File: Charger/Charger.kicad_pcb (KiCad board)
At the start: 2 copper layers, 100 x 100 mm, 189 parts, among them J1 Bat_ballanser_conn, J2 Battery_conn, J3 Power_conn, J4 Screen_SPInCtrlnPwr_Conn, J5 User_Interface_Conn, J8 Temp_Sens_Conn, Q1 BC846BW, Q10 MJD45H11T4, Q11 MJD45H11T4, Q12 MJD45H11T4, Q13 BC846BW, Q14 MJD31CT4, Q15 BUJ302AD, Q16 BUJ302AD, Q17 IRF7404, Q18 IRF7404, Q19 BC846BW, Q2 BC846BW, Q3 BC846BW, Q4 MJD45H11T4, Q5 MJD45H11T4, Q6 MJD45H11T4, Q7 BC846BW, Q8 BC846BW, Q9 BC846BW, U1 LM2904, U10 MCP6001-OT, U12 ACS712xLCTR-20A, U13 MCP6004, U17 XL4015, U18 XL4015, U19 MCP6001-OT, U2 LM2904, U20 LM2575-12BU, U21 L7805, U22 LDI1117-3.3, U23 RaspberryPi_Pico, U24 CD4051B, U25 MCP6004, U3 LM2904, U4 LM2904, U5 LM2904, U6 LM2904

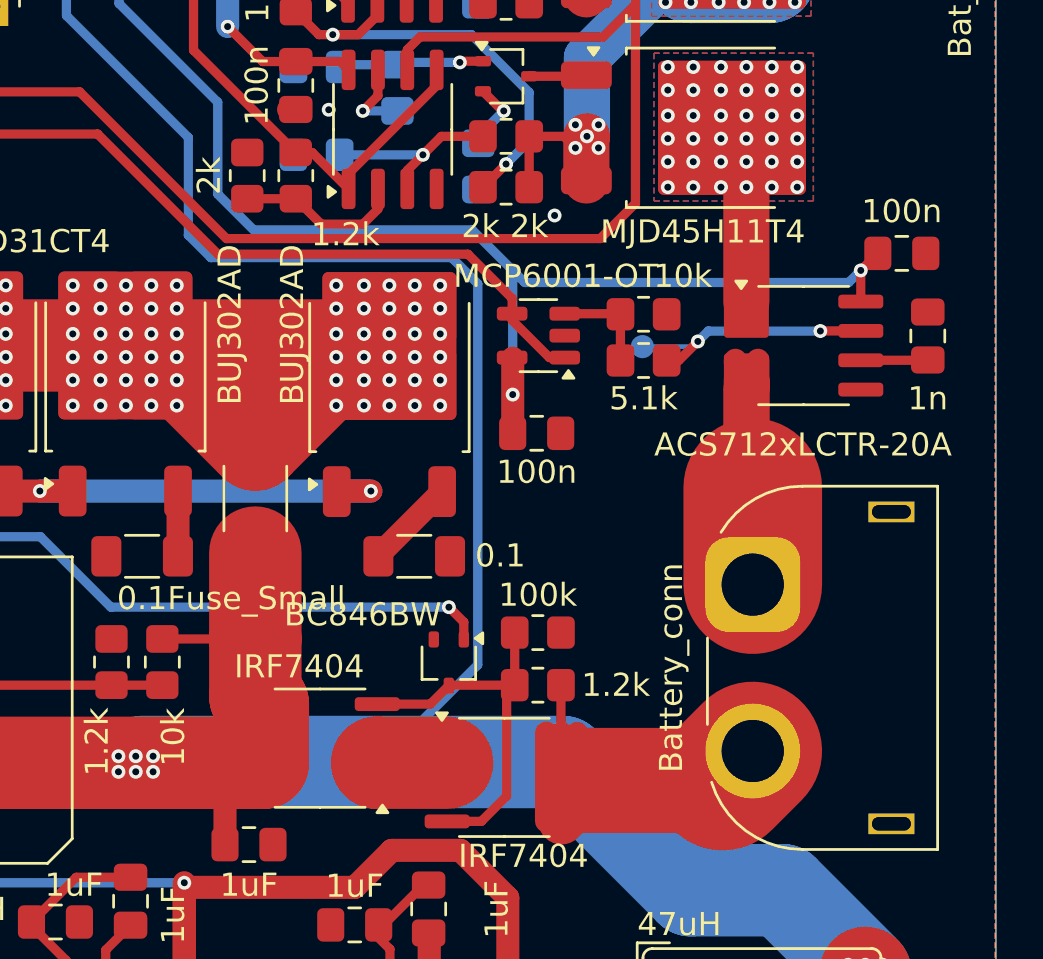
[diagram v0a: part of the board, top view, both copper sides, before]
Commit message: dodany hall od tylu i opisy
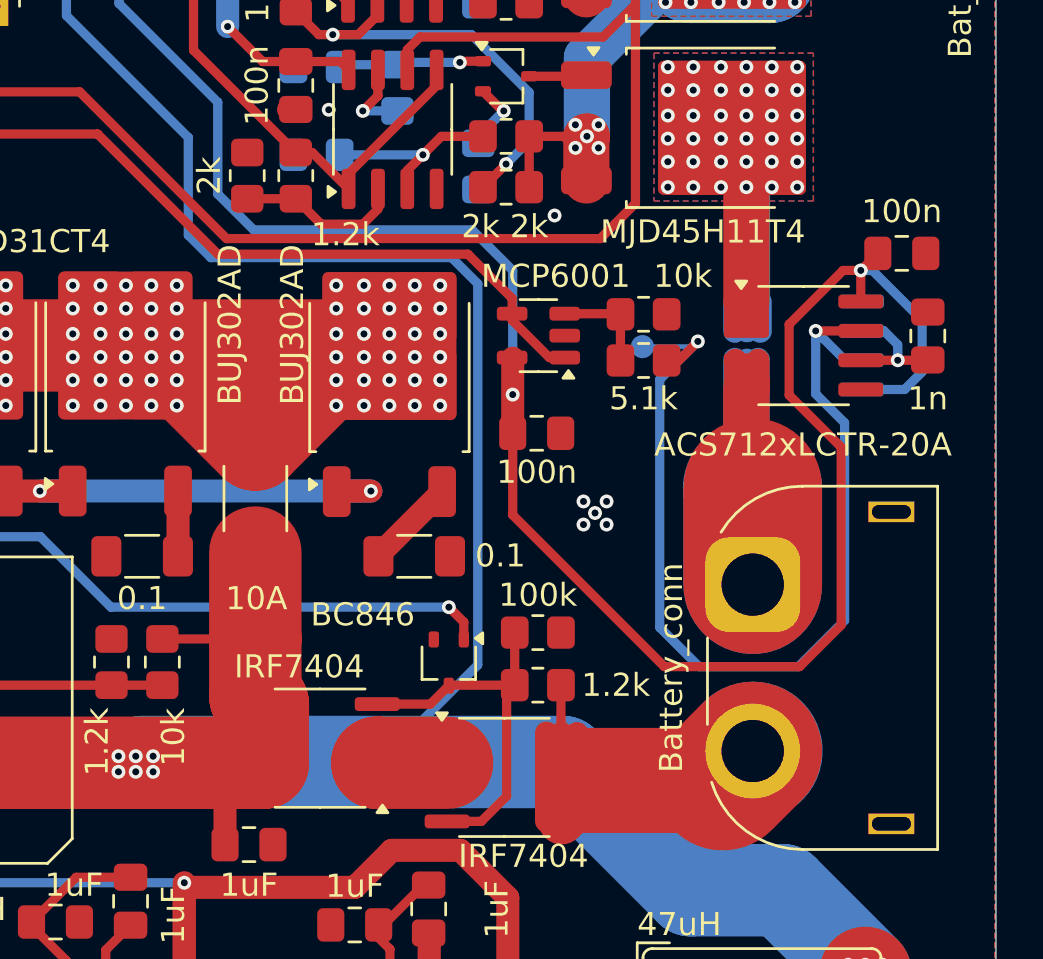
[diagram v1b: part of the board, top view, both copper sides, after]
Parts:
- added U7: ACS712xLCTR-20A, Package_SO:SOIC-8_3.9x4.9mm_P1.27mm, B.Cu at (184.7, 100.2)
- F2: value Fuse_Small -> 10A
- Q19: value BC846BW -> BC846
- U10: value MCP6001-OT -> MCP6001
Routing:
- net Net-(U12-VIOUT): track 11.4 -> 44.3 mm
- net +5V: track 282.8 -> 315.2 mm
- net /Pomiar pradu/BAT-: track 19.0 -> 31.4 mm
- net GND: track 48.0 -> 57.9 mm, vias 199 -> 204
- net Net-(U12-FILTER): track 2.91 -> 5.40 mm, vias 0 -> 1
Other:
- board text added: "+3.3V"
- board text added: "BL"
- board text added: "BTN_1"
- board text added: "BTN_2"
- board text added: "CS"
- board text added: "D/C"
- board text added: "ENC_CLK"
- board text added: "ENC_DT"
- board text added: "ENC_SW"
- board text added: "FMASK"
- board text added: "GND"
- board text added: "MISO"
- board text added: "MOSI"
- board text added: "RST"
- board text added: "SCK"

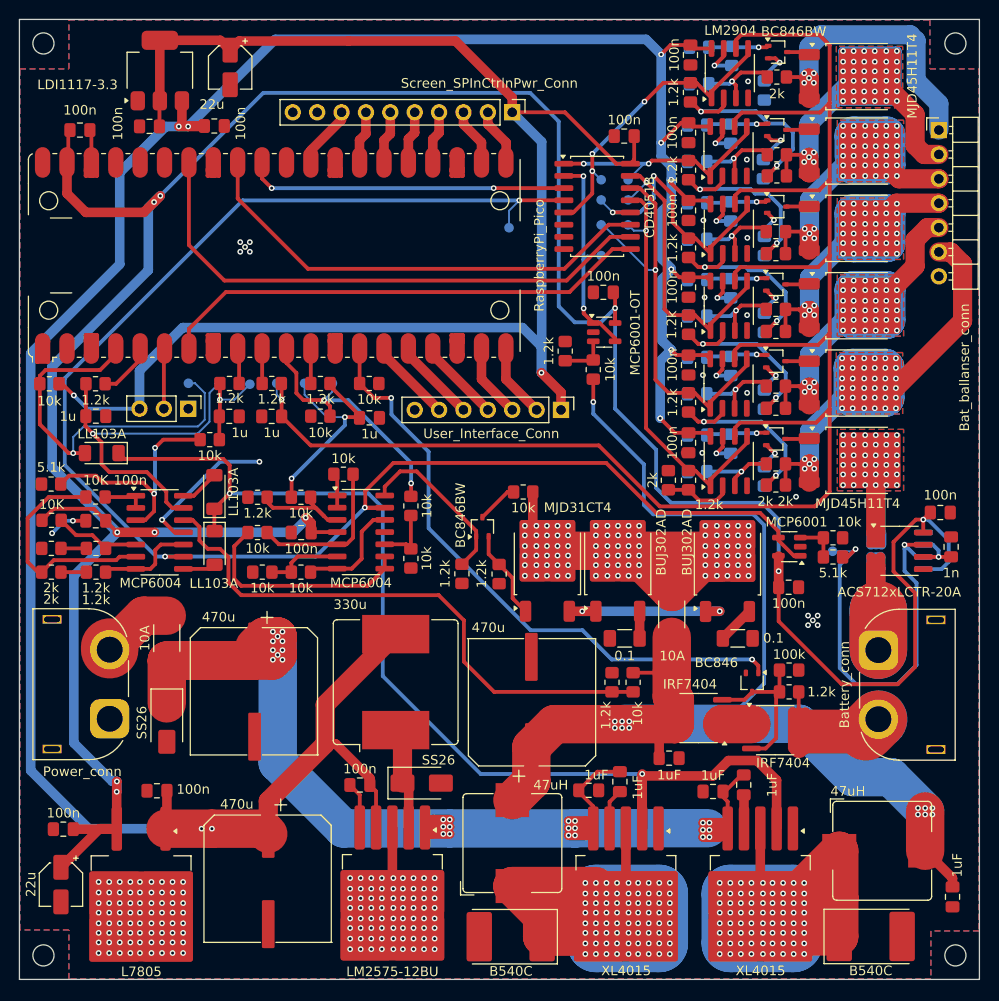
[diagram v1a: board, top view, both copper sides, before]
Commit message: up
zmienione kilka sciezek, dodane przelotki do masy i rezystor do adc
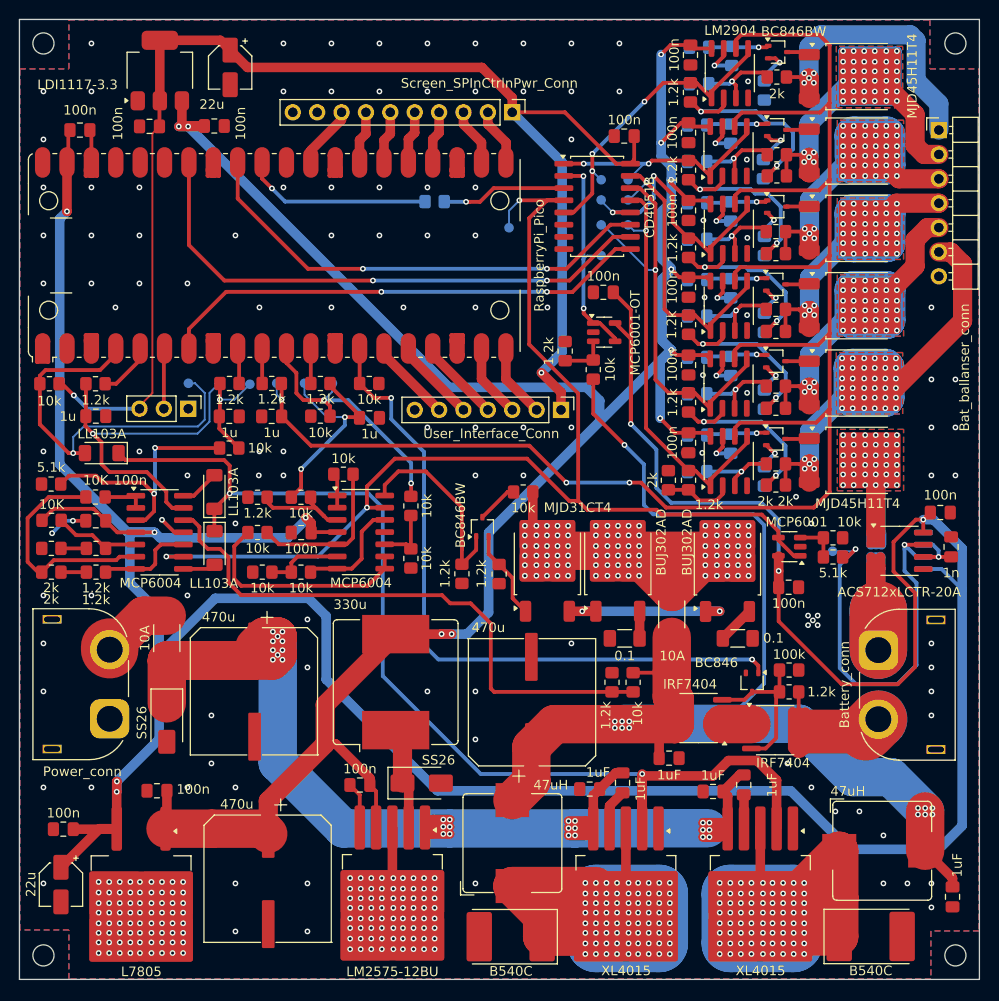
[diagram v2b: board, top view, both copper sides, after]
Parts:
- added R74: 10, Resistor_SMD:R_0805_2012Metric_Pad1.20x1.40mm_HandSolder, B.Cu at (136.2, 63.9)
- moved R61 2.21 mm to (114.8, 89.5)
- moved C19 0.30 mm to (155.8, 124.4)
- moved C16 0.16 mm to (152.4, 125.1), turned to 180 degrees
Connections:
- U24 pad 3: ADC_0 -> Net-(U24-X)
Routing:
- net +5V: track 315.2 -> 371.1 mm, vias 10 -> 8
- net +12V: track 283.4 -> 237.8 mm
- net /Ladowarka/Hall: track 168.2 -> 123.8 mm
- net +3.3V: track 161.8 -> 141.9 mm
- net ADC_0: track 35.9 -> 22.1 mm, vias 2 -> 1
- net Net-(U24-X): track 0.00 -> 13.1 mm, vias 0 -> 1
- net GND: track 57.9 -> 45.4 mm, vias 204 -> 303
- net GPIO10: track 68.5 -> 75.9 mm
- net Net-(Q13-B): track 17.8 -> 20.8 mm
- net +36V: track 136.9 -> 134.9 mm
- net Net-(U25A-+): track 25.6 -> 27.3 mm
- net /Ladowarka/Set I: track 9.84 -> 11.4 mm
- net Ref: track 59.1 -> 60.6 mm
- net /Balanser/Vballans: track 182.1 -> 182.2 mm, vias 1 -> 3
- net GPIO5: vias 0 -> 2
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
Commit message: PCB ostatecznie
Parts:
- removed the REF** at (190.5, 47.4)
- removed the REF** at (95.5, 142.4)
- removed the REF** at (95.5, 47.4)
- removed the REF** at (190.5, 142.4)
- added ?: , , F.Cu at (189.5, 141.4)
- added ?: , , F.Cu at (96.0, 47.9)
- added ?: , , F.Cu at (96.0, 91.9)
- added ?: , , F.Cu at (189.5, 89.9)
- added ?: , , F.Cu at (96.0, 141.9)
- added REF**: MountingHole_2.2mm_M2_DIN965_Pad_TopBottom, MountingHole:MountingHole_2.2mm_M2_DIN965_Pad_TopBottom, F.Cu at (189.5, 141.4)
- added REF**: MountingHole_2.2mm_M2_DIN965_Pad_TopBottom, MountingHole:MountingHole_2.2mm_M2_DIN965_Pad_TopBottom, F.Cu at (96.0, 47.9)
- added REF**: MountingHole_2.2mm_M2_DIN965_Pad_TopBottom, MountingHole:MountingHole_2.2mm_M2_DIN965_Pad_TopBottom, F.Cu at (96.0, 141.9)
- added REF**: MountingHole_2.2mm_M2_DIN965_Pad_TopBottom, MountingHole:MountingHole_2.2mm_M2_DIN965_Pad_TopBottom, F.Cu at (189.5, 89.9)
- added REF**: MountingHole_2.2mm_M2_DIN965_Pad_TopBottom, MountingHole:MountingHole_2.2mm_M2_DIN965_Pad_TopBottom, F.Cu at (96.0, 91.9)
- added REF**: MountingHole_2.2mm_M2_DIN965_Pad_TopBottom, MountingHole:MountingHole_2.2mm_M2_DIN965_Pad_TopBottom, F.Cu at (190.0, 47.9)
- moved R62 13.7 mm to (110.0, 92.4), turned to 180 degrees
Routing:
- net +5V: track 371.1 -> 385.2 mm, vias 8 -> 9
- net Net-(U25A-+): track 27.3 -> 18.7 mm, vias 2 -> 3
- net GND: vias 303 -> 302
